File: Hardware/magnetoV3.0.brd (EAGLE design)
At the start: 45.7 x 64.4 mm, 10 parts

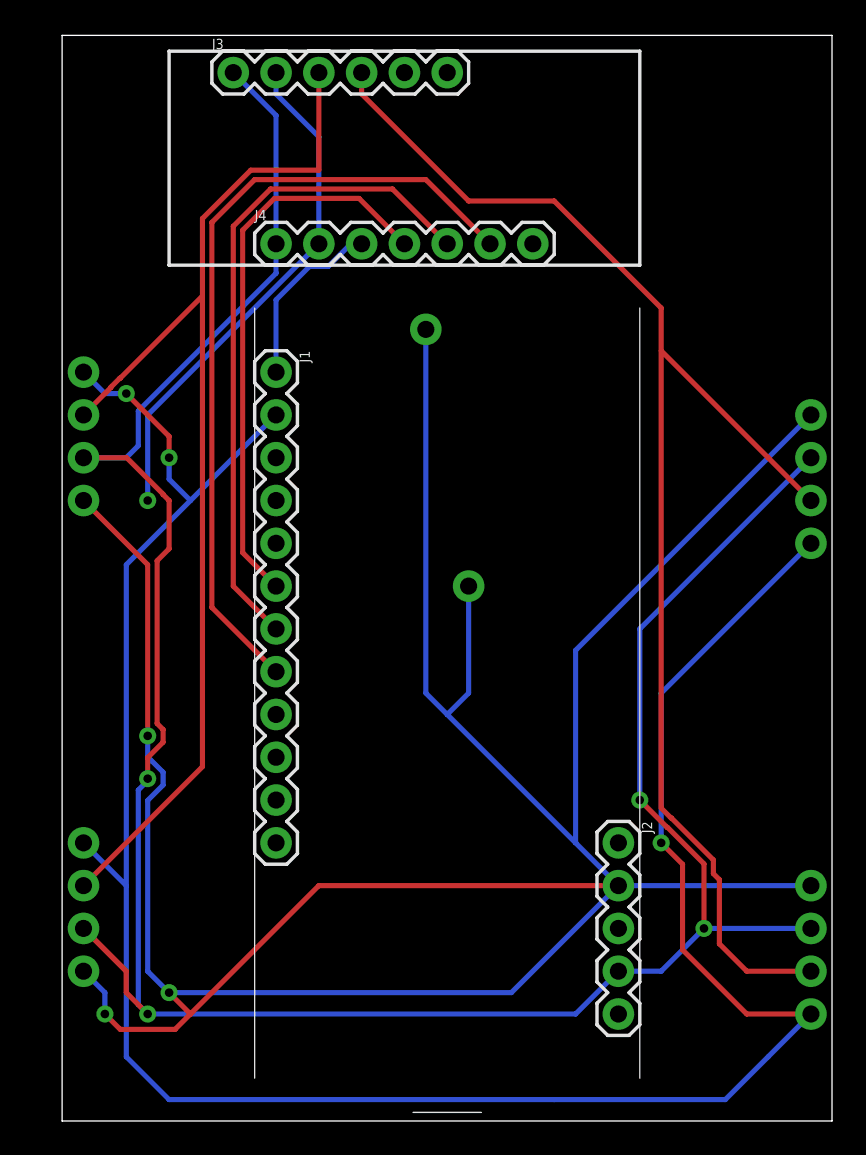
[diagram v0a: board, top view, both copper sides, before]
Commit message: PCB for the magneto board is complete. Send .brd file to Oshpark.
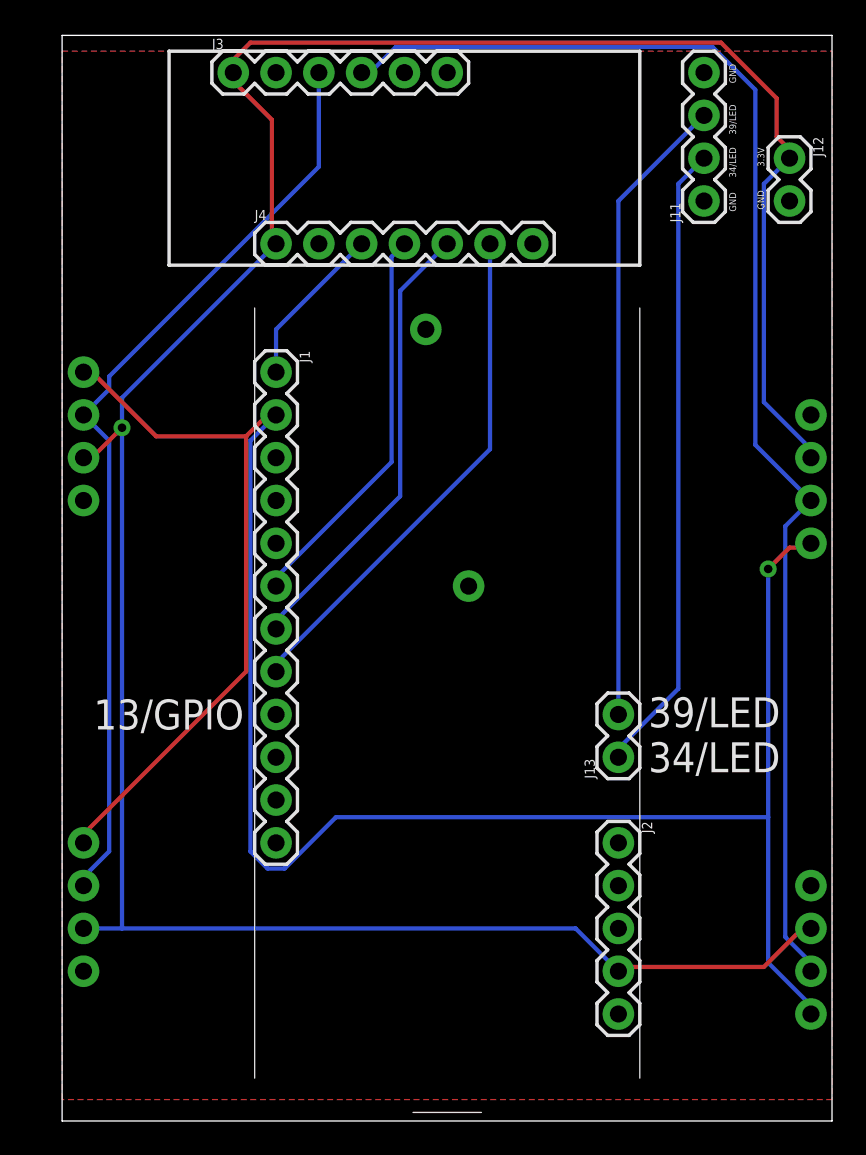
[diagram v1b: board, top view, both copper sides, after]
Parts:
- added J11: (no value), SparkFun-Connectors:1X04
- added J12, J13: (no value), SparkFun-Connectors:1X02
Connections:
- new net 13/GPIO: J1.9
- new net 34/LED: J11.2, J13.1
- new net 39/LED: J11.3, J13.2
- net 3.3V: now also J12.1
- net GND: now also J11.1, J11.4, J12.2
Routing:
- net GND: track 219.8 -> 0.00 mm, vias 4 -> 0
- net 39/LED: track 0.00 -> 37.7 mm
- net 34/LED: track 0.00 -> 37.7 mm
- net S2: track 47.4 -> 30.7 mm
- net S1: track 39.9 -> 27.1 mm
- net Y0/SDA: track 66.4 -> 55.3 mm
- net S0: track 33.4 -> 23.5 mm
- net 3.3V: track 153.5 -> 162.2 mm, vias 4 -> 1
- net SCL: track 137.7 -> 131.3 mm, vias 3 -> 1
- net Y1/SDA: track 82.2 -> 80.0 mm
- net Z/SDA: track 10.7 -> 9.72 mm
- added copper zone on layer 1, net GND
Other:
- board text added: "13/GPIO"
- board text added: "3.3V"
- board text added: "34/LED"
- board text added: "39/LED"
